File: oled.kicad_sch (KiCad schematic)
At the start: 1 part

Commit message: First OLED idea
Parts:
- added DS2: OLED-128O064D, Display:OLED-128O064D, symbol Display_Graphic:OLED-128O064D
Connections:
- new net: DS2.1 (GND), DS2.30 (GND)
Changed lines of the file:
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@@
+		)
+	)
+	(symbol
+		(lib_id "Display_Graphic:OLED-128O064D")
+		(at 182.88 74.93 0)
+		(unit 1)
+		(exclude_from_sim no)
+		(in_bom yes)
+		(on_board yes)
+		(dnp no)
+		(fields_autoplaced yes)
+		(property "Reference" "DS2"
+			(at 194.31 73.6599 0)
+			(effects
+				(font
+					(size 1.27 1.27)
+				)
+				(justify left)
+			)
+		)
+		(property "Value" "OLED-128O064D"
+			(at 194.31 76.1999 0)
+			(effects
+				(font
+					(size 1.27 1.27)
+				)
+				(justify left)
+			)
+		)
+		(property "Footprint" "Display:OLED-128O064D"
+			(at 182.88 74.93 0)
+			(effects
+				(font
+					(size 1.27 1.27)
+				)
+				(hide yes)
+			)
+		)
+		(property "Datasheet" "https://www.vishay.com/docs/37902/oled128o064dbpp3n00000.pdf"
+			(at 182.88 54.61 0)
+			(effects
+				(font
+					(size 1.27 1.27)
+				)
+				(hide yes)
+			)
+		)
+		(property "Description" "OLED display 128x64"
+			(at 182.88 74.93 0)
+			(effects
+				(font
+					(size 1.27 1.27)
+				)
+				(hide yes)
+			)
+		)
+		(pin "8"
+		)
+		(pin "4"
+		)
+		(pin "3"
+		)
+		(pin "7"
+		)
+		(pin "30"
+		)
+		(pin "25"
+		)
+		(pin "13"
+		)
+		(pin "14"
+		)
+		(pin "29"
+		)
+		(pin "11"
+		)
+		(pin "10"
+		)
+		(pin "19"
+		)
+		(pin "23"
+		)
+		(pin "15"
+		)
+		(pin "24"
+		)
+		(pin "28"
+		)
+		(pin "6"
+		)
+		(pin "5"
+		)
+		(pin "16"
+		)
+		(pin "1"
+		)
+		(pin "2"
+		)
+		(pin "27"
+		)
+		(pin "26"
+		)
+		(pin "9"
+		)
+		(pin "22"
+		)
+		(pin "21"
+		)
+		(pin "17"
+		)
+		(pin "12"
+		)
+		(pin "18"
+		)
+		(pin "20"
+		)
+		(instances
+			(project ""
+				(path "/02aefeb1-bdda-4e04-a64a-6cb1fcf66702/48841d67-bf6b-46ea-91fc-8a4fa6e7a591"
+					(reference "DS2")
+					(unit 1)
+				)
+			)
 		)
 	)

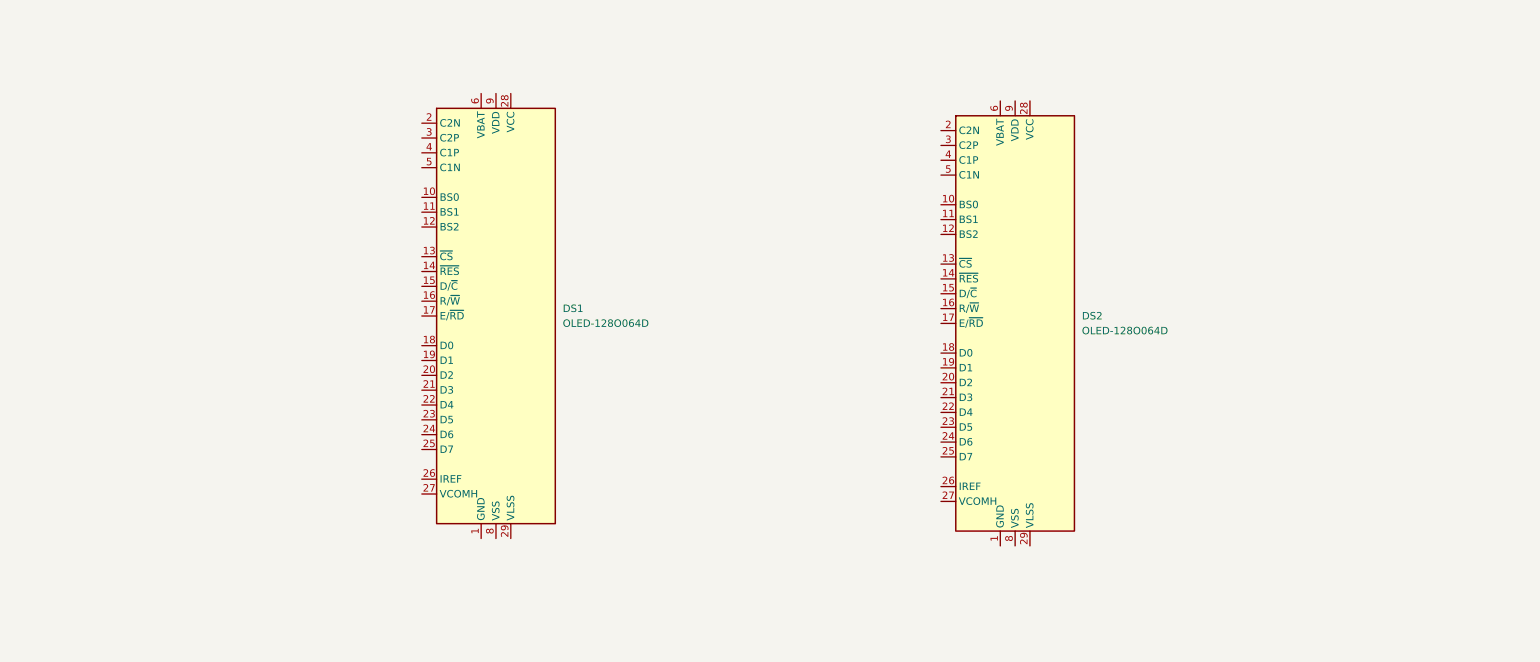
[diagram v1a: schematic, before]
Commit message: First OLED wiring
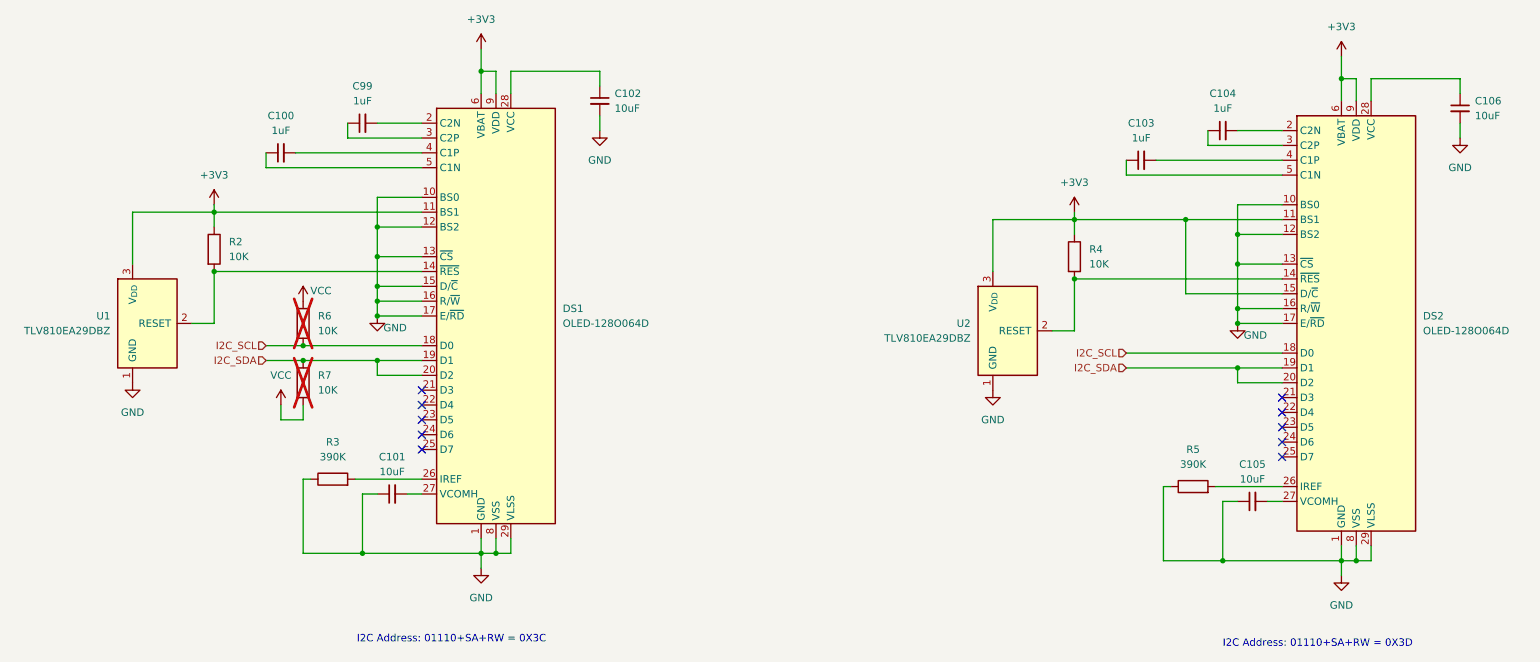
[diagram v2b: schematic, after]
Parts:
- added C100, C103, C104, C99: 1uF, symbol Device:C_Small
- added C101, C102, C105, C106: 10uF, symbol Device:C_Small
- added R2, R4, R6, R7: 10K, symbol Device:R
- added R3, R5: 390K, symbol Device:R
- added U1, U2: TLV810EA29DBZ, Package_TO_SOT_SMD:SOT-23, symbol Power_Supervisor:TLV810EA29DBZ
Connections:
- net GND: now reaches DS1.1 (GND), DS1.30 (GND)
- net GND: now also DS1.10 (BS0), DS1.12 (BS2), DS1.13 (~{CS}), DS1.15 (D/~{C}), DS1.16 (R/~{W}), DS1.17 (E/~{RD}), DS1.29 (VLSS), DS1.8 (VSS), DS2.1 (GND), DS2.10 (BS0), DS2.12 (BS2), DS2.13 (~{CS}), DS2.16 (R/~{W}), DS2.17 (E/~{RD}), DS2.29 (VLSS), DS2.30 (GND), DS2.8 (VSS), C101.1, C102.2, C105.1, C106.2, R3.1, R5.1, U1.1 (GND), U2.1 (GND)
- net +3V3: now reaches DS1.11 (BS1)
- net +3V3: now also DS1.6 (VBAT), DS1.9 (VDD), DS2.11 (BS1), DS2.15 (D/~{C}), DS2.6 (VBAT), DS2.9 (VDD), R2.1, R4.1, U1.3 (V_{DD}), U2.3 (V_{DD})
- net at DS1.14 (~{RES}): now also R2.2, U1.2 (RESET)
- net I2C_SCL: now reaches DS1.18 (D0)
- net I2C_SCL: now also DS2.18 (D0), R6.2
- net I2C_SDA: now reaches DS1.19 (D1)
- net I2C_SDA: now also DS1.20 (D2), DS2.19 (D1), DS2.20 (D2), R7.1
- net at DS1.2 (C2N): now also C99.2
- net at DS1.26 (IREF): now also R3.2
- net at DS1.27 (VCOMH): now also C101.2
- net at DS1.28 (VCC): now also C102.1
- net at DS1.3 (C2P): now also C99.1
- net at DS1.4 (C1P): now also C100.2
- net at DS1.5 (C1N): now also C100.1
- net at DS2.14 (~{RES}): now also R4.2, U2.2 (RESET)
- net at DS2.2 (C2N): now also C104.2
- net at DS2.26 (IREF): now also R5.2
- net at DS2.27 (VCOMH): now also C105.2
- net at DS2.28 (VCC): now also C106.1
- net at DS2.3 (C2P): now also C104.1
- net at DS2.4 (C1P): now also C103.2
- net at DS2.5 (C1N): now also C103.1
- new net VCC: R6.1, R7.2
- no-connect marks 0 -> 10
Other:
- note added: "I2C Address: 01110+SA+RW = 0X3C"
- note added: "I2C Address: 01110+SA+RW = 0X3D"
- company: (none) -> https://github.com/pedalboard
- title: (none) -> Pedalboard Display

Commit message: Only use one reset circuit
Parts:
- removed R4: 10K, symbol Device:R
- removed U2: TLV810EA29DBZ, Package_TO_SOT_SMD:SOT-23, symbol Power_Supervisor:TLV810EA29DBZ
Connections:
- net RES: now reaches DS1.14 (~{RES}), R2.2, U1.2 (RESET)
- net RES: now also DS2.14 (~{RES})
